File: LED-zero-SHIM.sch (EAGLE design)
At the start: 147 parts

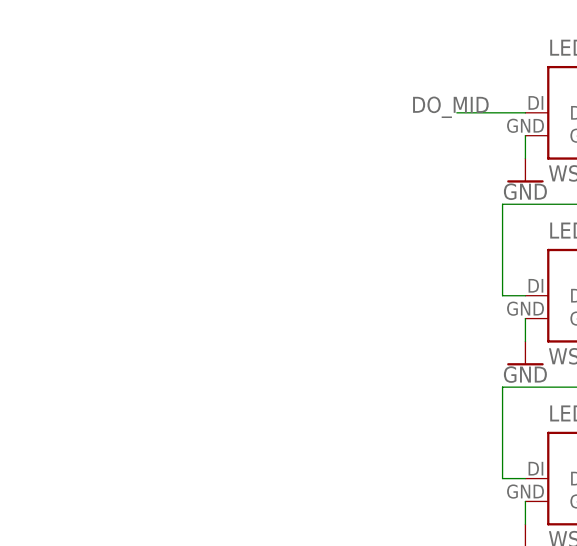
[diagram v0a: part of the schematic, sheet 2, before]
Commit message: added buffer and caps
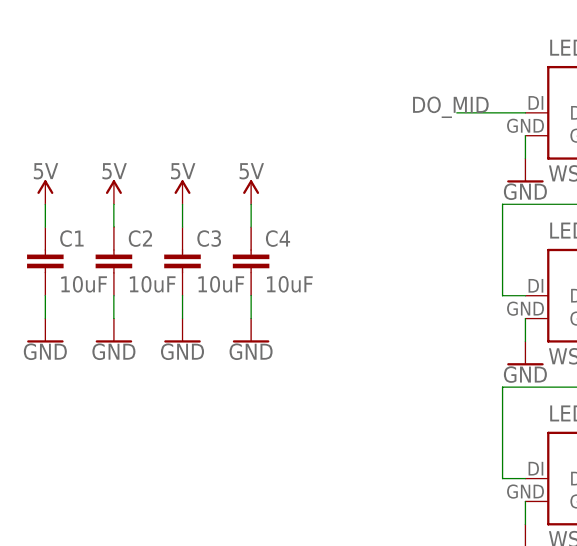
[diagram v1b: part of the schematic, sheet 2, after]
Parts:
- added C1, C2, C3, C4: 10uF, rcl:C-EUC0805
- added IC1: TXB0101DCKR, TXB0101DCKR:TXB0101DCKR
- added R1: (no value), rcl:R-EU_R0402
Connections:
- new net DATA: IC1.A
- new net N$143: IC1.OE, R1.2
- net 3.3V: now also IC1.VCCA, R1.1
- net 5V: now also C1.1, C2.1, C3.1, C4.1, IC1.VCCB
- net DI_FIRST: now also IC1.B
- net GND: now also C1.2, C2.2, C3.2, C4.2, IC1.GND

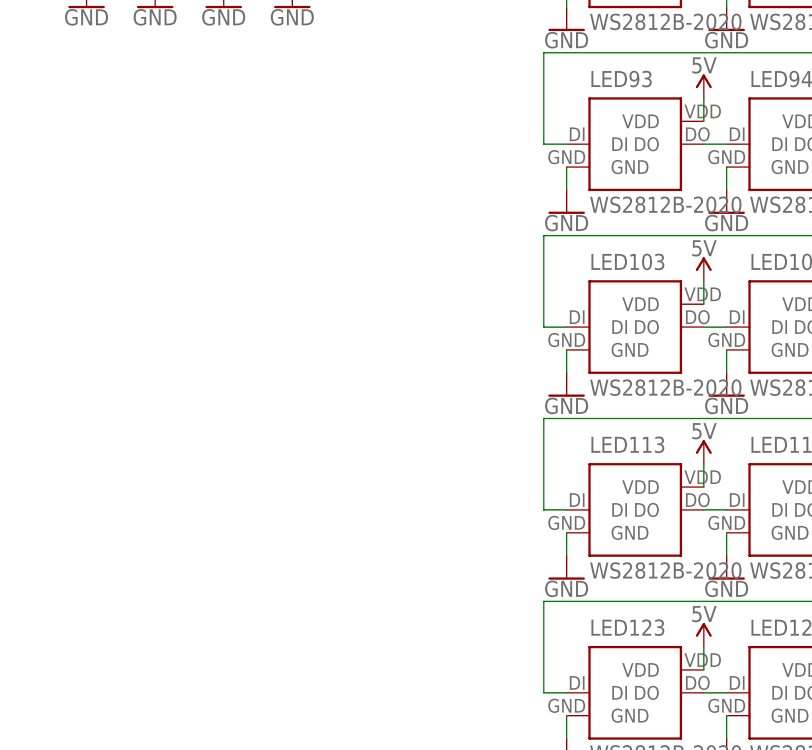
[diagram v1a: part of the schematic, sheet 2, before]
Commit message: Added solder joint for DATA input configuration
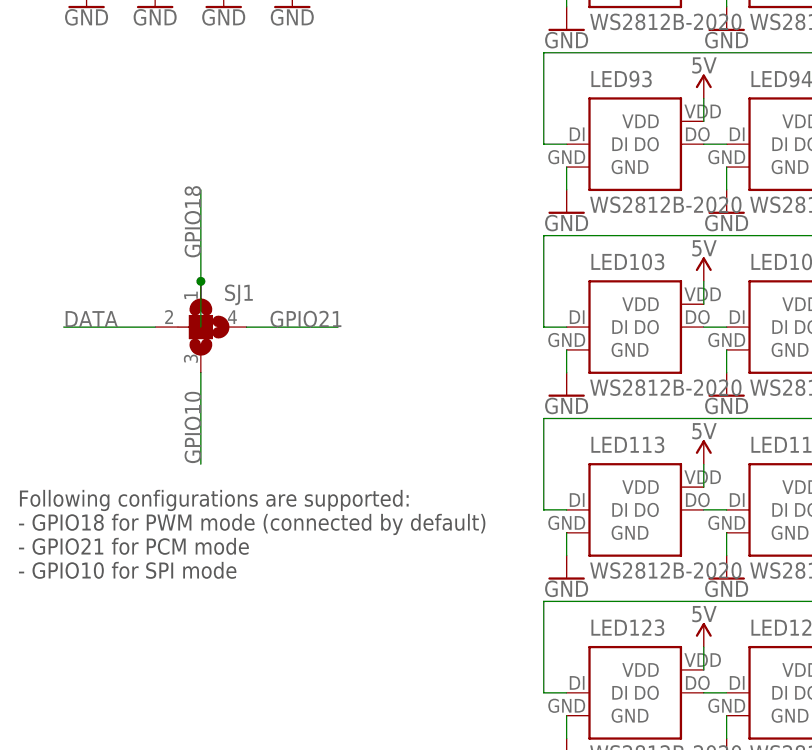
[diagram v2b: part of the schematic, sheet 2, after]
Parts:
- added SJ1: (no value), _my_jumpers:SJ3
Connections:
- net DATA: now also SJ1.2
- net GPIO10: now also SJ1.3
- net GPIO18: now also SJ1.1
- net GPIO21: now also SJ1.4
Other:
- note added: "Following configurations are supported: - GPIO18 for PWM mode (connected by default) - GPIO21 for PCM mode - GPIO10 for SPI mode"
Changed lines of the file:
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@@
 <part name="SUPPLY154" library="SparkFun-PowerSymbols" library_urn="urn:adsk.eagle:library:530" deviceset="5V" device=""/>
 <part name="GND151" library="SparkFun-PowerSymbols" library_urn="urn:adsk.eagle:library:530" deviceset="GND" device=""/>
+<part name="SJ1" library="_my_jumpers" deviceset="SJ3" device=""/>
 </parts>
 <sheets>
@@
 <text x="165.1" y="25.4" size="2.54" layer="94">Pi Zero sized LED-SHIM for Pi's 40-pin extension slot
 (c) Andriy Golovnya</text>
+<text x="10.16" y="71.12" size="1.778" layer="97">Following configurations are supported:
+- GPIO18 for PWM mode (connected by default)
+- GPIO21 for PCM mode
+- GPIO10 for SPI mode</text>
 </plain>
 <instances>
@@
 <attribute name="VALUE" x="40.64" y="134.366" size="1.778" layer="96" align="top-center"/>
 </instance>
+<instance part="SJ1" gate="G$1" x="30.48" y="99.06" smashed="yes">
+<attribute name="NAME" x="33.02" y="101.981" size="1.778" layer="95"/>
+<attribute name="VALUE" x="33.02" y="94.615" size="1.778" layer="96"/>
+</instance>
 </instances>
 <busses>
@@
 </segment>
 </net>
+<net name="GPIO21" class="0">
+<segment>
+<pinref part="SJ1" gate="G$1" pin="4"/>
+<wire x1="35.56" y1="99.06" x2="45.72" y2="99.06" width="0.1524" layer="91"/>
+<label x="38.1" y="99.06" size="1.778" layer="95"/>
+</segment>
+</net>
+<net name="DATA" class="0">
+<segment>
+<pinref part="SJ1" gate="G$1" pin="2"/>
+<wire x1="25.4" y1="99.06" x2="15.24" y2="99.06" width="0.1524" layer="91"/>
+<label x="15.24" y="99.06" size="1.778" layer="95"/>
+</segment>
+</net>
+<net name="GPIO18" class="0">
+<segment>
+<pinref part="SJ1" gate="G$1" pin="1"/>
+<wire x1="30.48" y1="104.14" x2="30.48" y2="114.3" width="0.1524" layer="91"/>
+<label x="30.48" y="106.68" size="1.778" layer="95" rot="R90"/>
+<wire x1="30.48" y1="104.14" x2="30.48" y2="99.06" width="0.1524" layer="91"/>
+<junction x="30.48" y="104.14"/>
+</segment>
+</net>
+<net name="GPIO10" class="0">
+<segment>
+<pinref part="SJ1" gate="G$1" pin="3"/>
+<wire x1="30.48" y1="93.98" x2="30.48" y2="83.82" width="0.1524" layer="91"/>
+<label x="30.48" y="83.82" size="1.778" layer="95" rot="R90"/>
+</segment>
+</net>

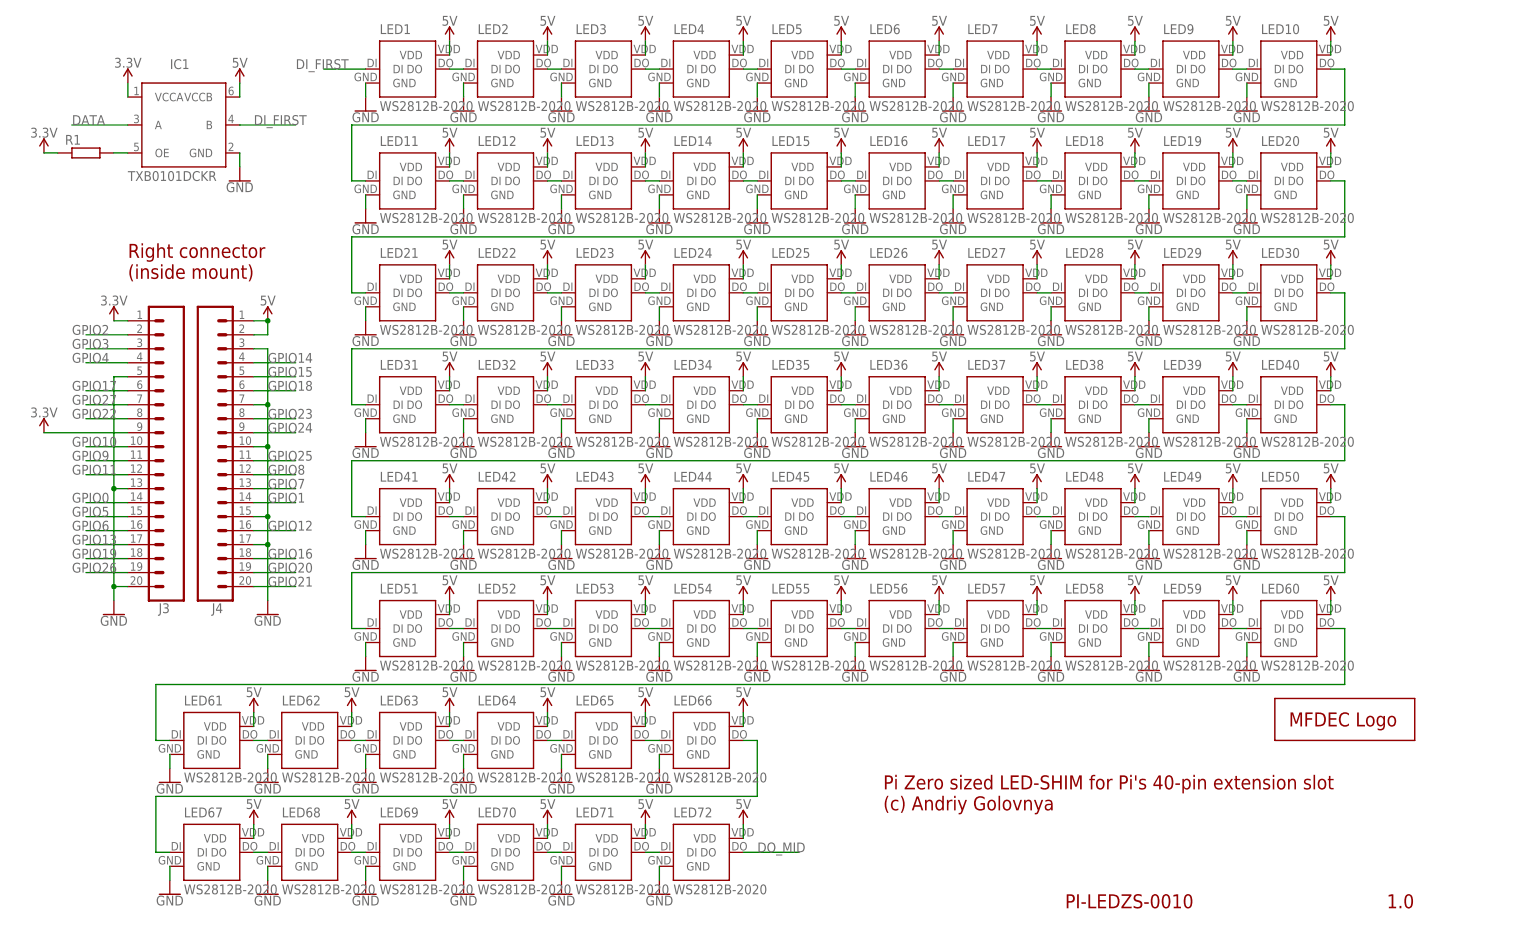
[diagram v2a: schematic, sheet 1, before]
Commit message: Use C veriant of LED insted of B.
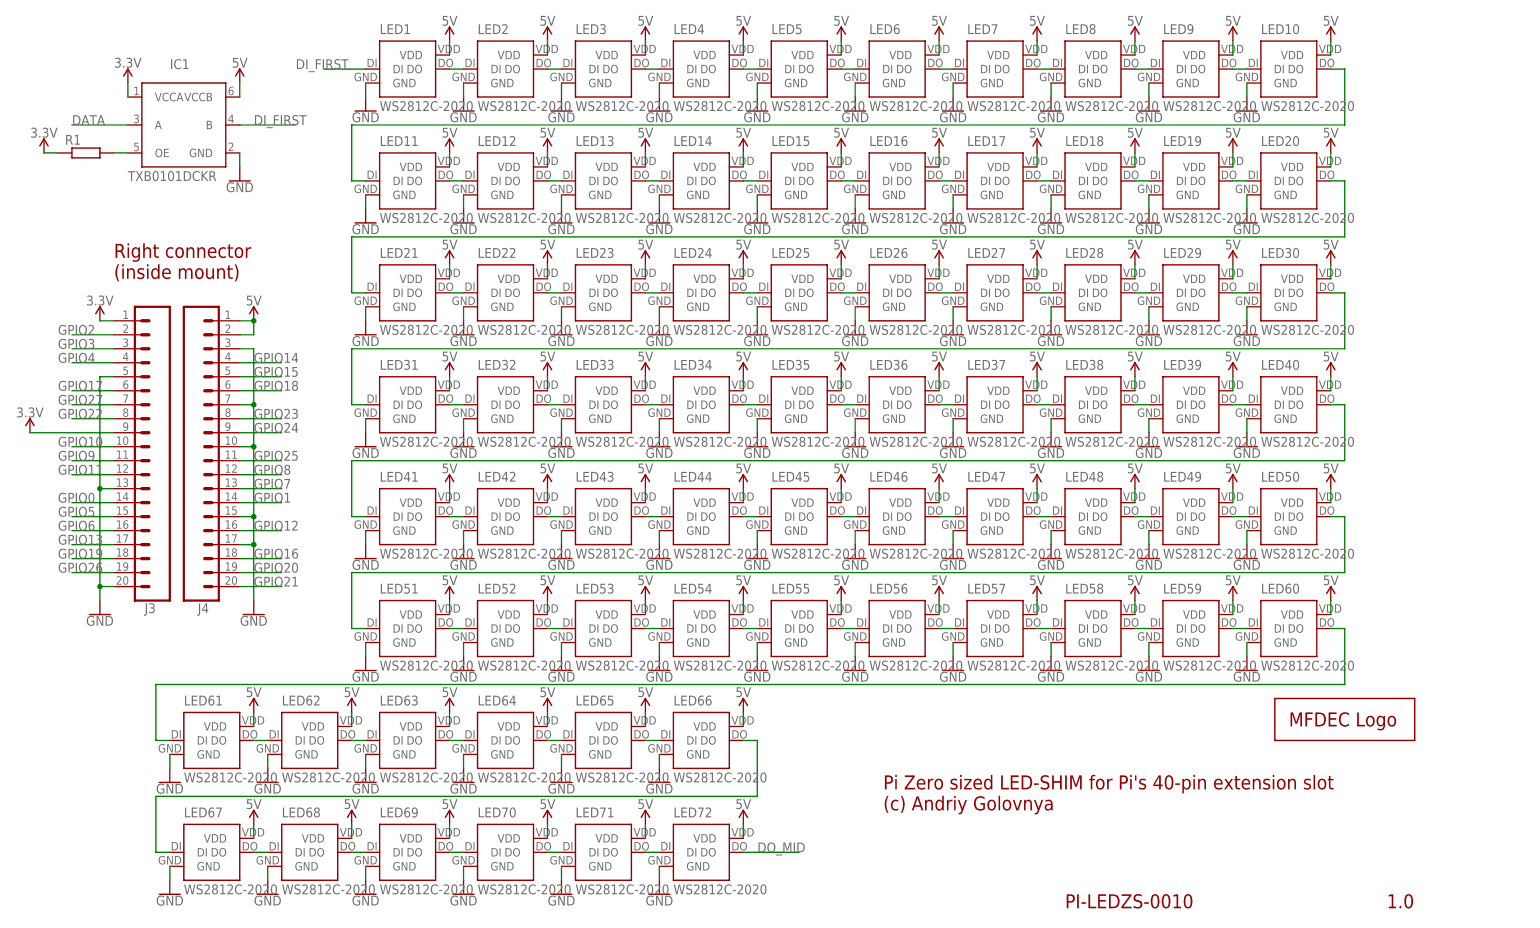
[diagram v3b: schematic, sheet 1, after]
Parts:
- added J1, J2: (no value), SparkFun-Connectors:CONN_03
- LED1, LED10, LED100, LED101, LED102, LED103, LED104, LED105, LED106, LED107, LED108, LED109, LED11, LED110, LED111, LED112, LED113, LED114, LED115, LED116, LED117, LED118, LED119, LED12, LED120, LED121, LED122, LED123, LED124, LED125, LED126, LED127, LED128, LED129, LED13, LED130, LED131, LED132, LED133, LED134, LED135, LED136, LED137, LED138, LED139, LED14, LED140, LED141, LED142, LED143, LED144, LED15, LED16, LED17, LED18, LED19, LED2, LED20, LED21, LED22, LED23, LED24, LED25, LED26, LED27, LED28, LED29, LED3, LED30, LED31, LED32, LED33, LED34, LED35, LED36, LED37, LED38, LED39, LED4, LED40, LED41, LED42, LED43, LED44, LED45, LED46, LED47, LED48, LED49, LED5, LED50, LED51, LED52, LED53, LED54, LED55, LED56, LED57, LED58, LED59, LED6, LED60, LED61, LED62, LED63, LED64, LED65, LED66, LED67, LED68, LED69, LED7, LED70, LED71, LED72, LED73, LED74, LED75, LED76, LED77, LED78, LED79, LED8, LED80, LED81, LED82, LED83, LED84, LED85, LED86, LED87, LED88, LED89, LED9, LED90, LED91, LED92, LED93, LED94, LED95, LED96, LED97, LED98, LED99: value WS2812B-2020 -> WS2812C-2020; device WS2812B-2020:WS2812B-2020 -> WS281X:WS2812C-2020
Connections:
- net 5V: now also J1.3, J2.3
- net DI_FIRST: now also J1.2
- net DO_LAST: now also J2.2
- net GND: now also J1.1, J2.1
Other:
- moved on the sheet: C1, C2, C3, C4, J3, J4, SJ1

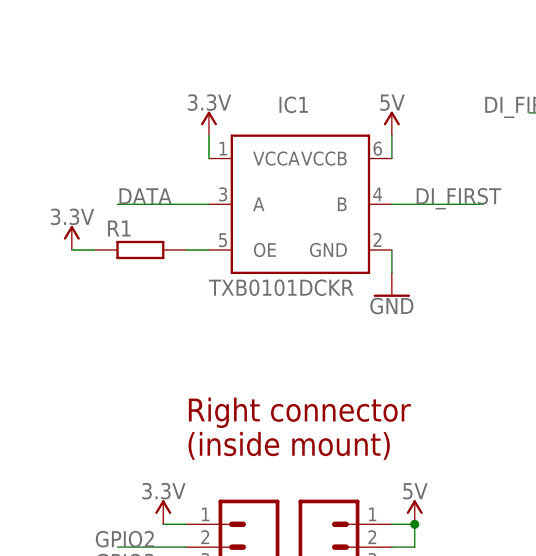
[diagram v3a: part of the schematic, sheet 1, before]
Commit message: Added some traces.
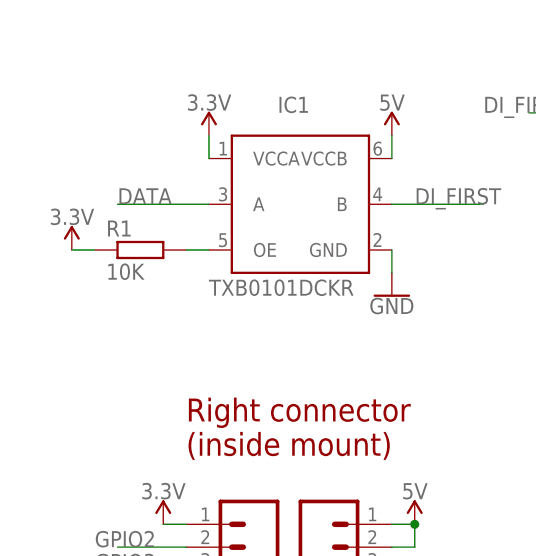
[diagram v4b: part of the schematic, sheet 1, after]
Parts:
- R1: value (none) -> 10K
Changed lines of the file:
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@@
 <part name="SUPPLY149" library="SparkFun-PowerSymbols" library_urn="urn:adsk.eagle:library:530" deviceset="5V" device=""/>
 <part name="GND147" library="SparkFun-PowerSymbols" library_urn="urn:adsk.eagle:library:530" deviceset="GND" device=""/>
-<part name="R1" library="rcl" library_urn="urn:adsk.eagle:library:334" deviceset="R-EU_" device="R0402" package3d_urn="urn:adsk.eagle:package:23547/3"/>
+<part name="R1" library="rcl" library_urn="urn:adsk.eagle:library:334" deviceset="R-EU_" device="R0402" package3d_urn="urn:adsk.eagle:package:23547/3" value="10K"/>
 <part name="SUPPLY150" library="SparkFun-PowerSymbols" library_urn="urn:adsk.eagle:library:530" deviceset="3.3V" device=""/>
 <part name="C1" library="rcl" library_urn="urn:adsk.eagle:library:334" deviceset="C-EU" device="C0805" package3d_urn="urn:adsk.eagle:package:23617/2" value="10uF"/>
@@
 </sheet>
 </sheets>
+<errors>
+</errors>
 </schematic>
 </drawing>

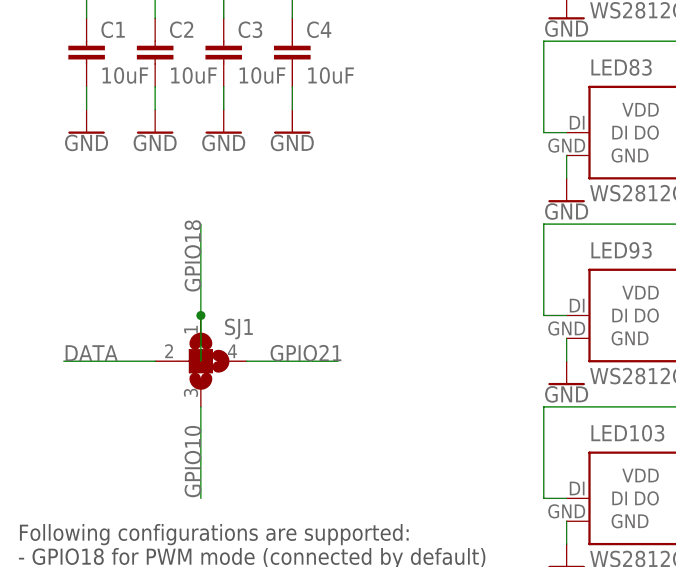
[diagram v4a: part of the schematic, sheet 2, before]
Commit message: Made the board 4-layer and routed it completely.
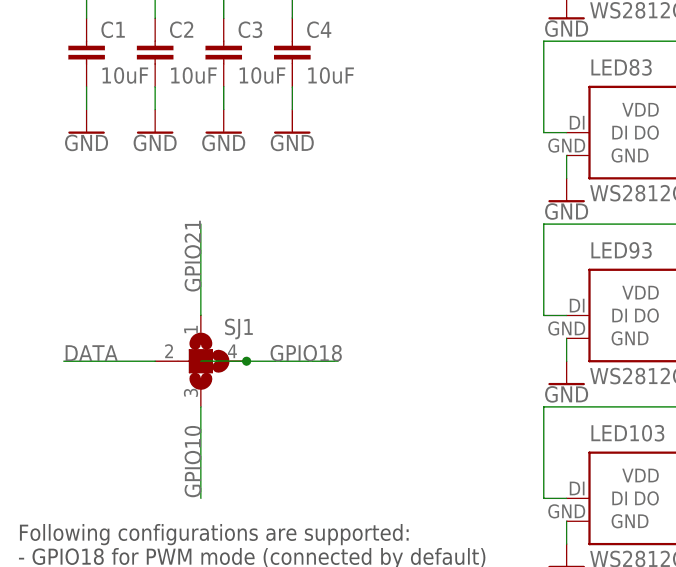
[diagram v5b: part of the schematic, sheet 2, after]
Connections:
- net GPIO18: now also SJ1.4; no longer SJ1.1
- net GPIO21: now also SJ1.1; no longer SJ1.4
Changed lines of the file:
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@@
 <net name="GPIO21" class="0">
 <segment>
-<pinref part="SJ1" gate="G$1" pin="4"/>
-<wire x1="35.56" y1="114.3" x2="45.72" y2="114.3" width="0.1524" layer="91"/>
-<label x="38.1" y="114.3" size="1.778" layer="95"/>
+<pinref part="SJ1" gate="G$1" pin="1"/>
+<wire x1="30.48" y1="119.38" x2="30.48" y2="129.54" width="0.1524" layer="91"/>
+<label x="30.48" y="121.92" size="1.778" layer="95" rot="R90"/>
 </segment>
 </net>
@@
 <wire x1="25.4" y1="114.3" x2="15.24" y2="114.3" width="0.1524" layer="91"/>
 <label x="15.24" y="114.3" size="1.778" layer="95"/>
-</segment>
-</net>
-<net name="GPIO18" class="0">
-<segment>
-<pinref part="SJ1" gate="G$1" pin="1"/>
-<wire x1="30.48" y1="119.38" x2="30.48" y2="129.54" width="0.1524" layer="91"/>
-<label x="30.48" y="121.92" size="1.778" layer="95" rot="R90"/>
-<wire x1="30.48" y1="119.38" x2="30.48" y2="114.3" width="0.1524" layer="91"/>
-<junction x="30.48" y="119.38"/>
 </segment>
 </net>
@@
 </segment>
 </net>
+<net name="GPIO18" class="0">
+<segment>
+<pinref part="SJ1" gate="G$1" pin="4"/>
+<wire x1="35.56" y1="114.3" x2="45.72" y2="114.3" width="0.1524" layer="91"/>
+<label x="38.1" y="114.3" size="1.778" layer="95"/>
+<wire x1="35.56" y1="114.3" x2="30.48" y2="114.3" width="0.1524" layer="91"/>
+<junction x="35.56" y="114.3"/>
+</segment>
+</net>
